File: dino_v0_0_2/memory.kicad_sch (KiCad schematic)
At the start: 5 parts, among them U19 74LS245, U21 74LS245, U24 AT28C256, U26 MCM60256AP, U51 7400

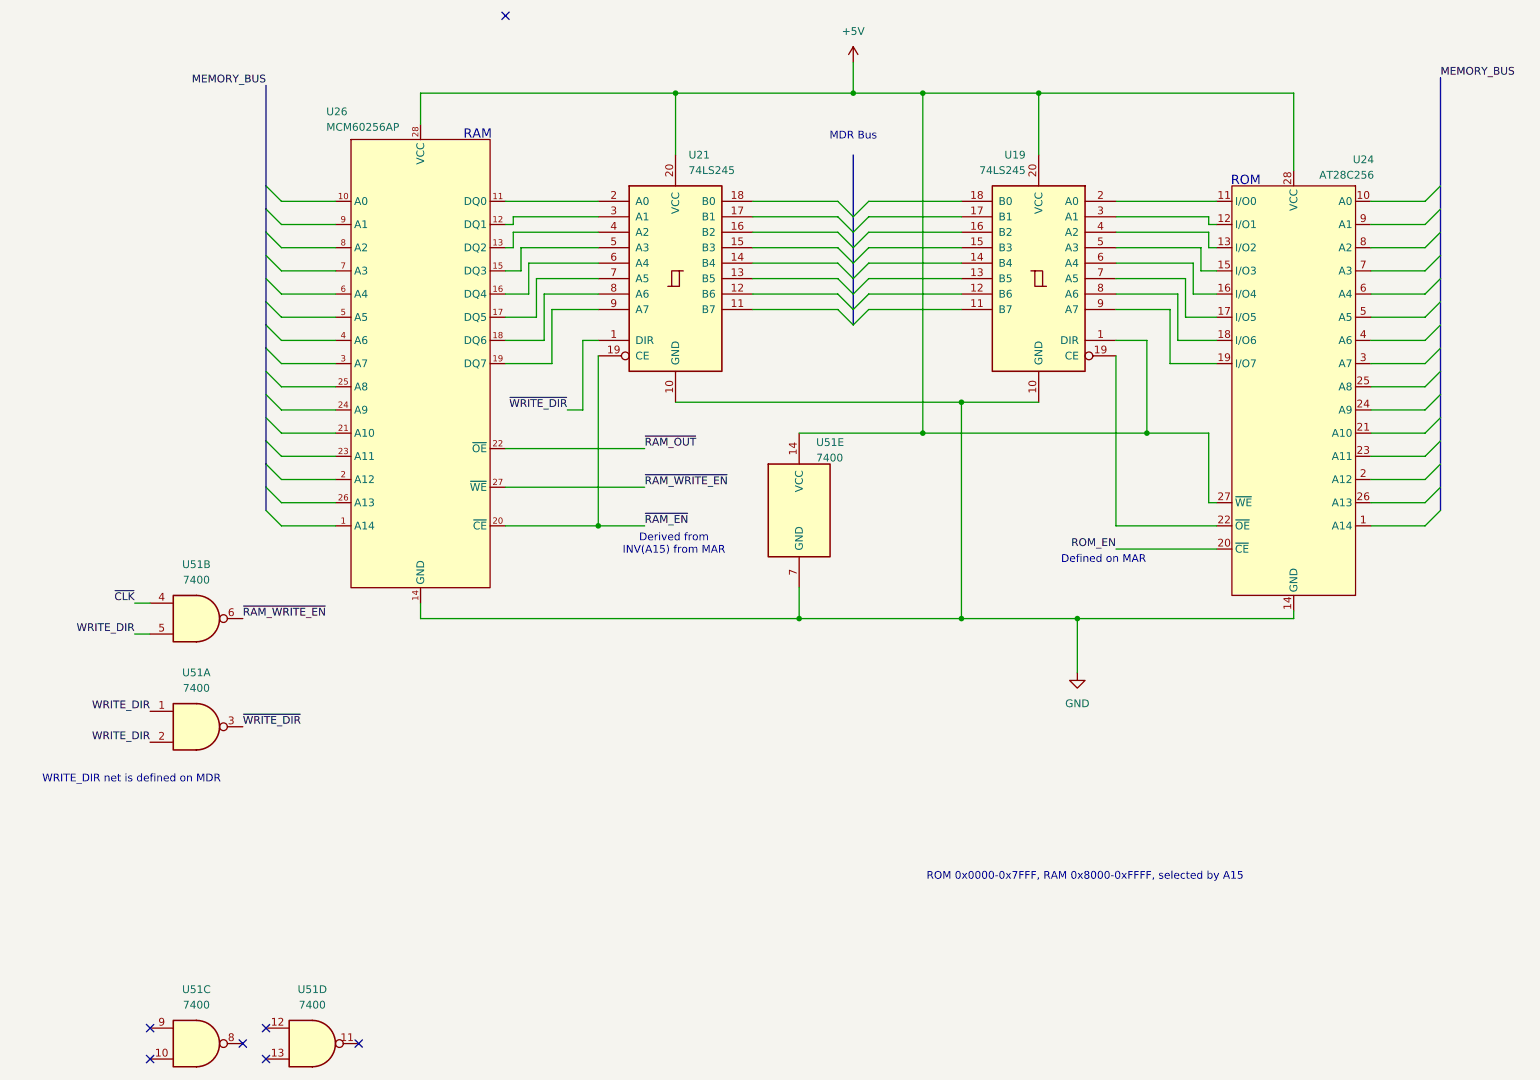
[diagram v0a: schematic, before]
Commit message: DINO v0.0.3: complete ALU/control-word, add MAR+reset sheets, wire reset circuit
ALU sheet: flags register moved from '173 (not in stock) to '273 + a '157
mux to emulate the missing load-enable pins; Z-detect built from a NOR+AND
De Morgan tree instead of a '260; ALU_CIN built from NAND(SA1,SA0) reusing
two already-placed spare gates instead of a dedicated XOR/'86. Sheet is
now fully wired and netlist-clean.

Control word sheet: all 16 CW bits assigned and wired (3x '138 decoders
for the load/source/misc fields, direct bus taps for HALT/PC_MAR_MUX/
PC_UP/END and the ALU SA[2:0] select). Found and fixed several cross-
sheet signal-name mismatches this uncovered (OUT_REG_LOAD/REG_OUT_LOAD,
PC_MAR_MUX/PC_MUX, T-state counter labels, a mirror-reversed IRB->ROM-
address buffer in microcode).

New: MAR and reset sheets, wired into the root hierarchy. Reset circuit
is a from-scratch design: RC+button+74HC14 Schmitt front end feeds the
async PRESET of the clock cluster's spare '74 half (U27B), synchronizing
release to CLK; its Q/~Q fan out to the flags register, the T-state
counter's clear, and (OR'd with the existing microcode-driven PC_CLEAR,
reusing spare gates on the same '02) the PC counters' clear.

Deprecated 7 schematic files no longer referenced by the root sheet's
hierarchy into dino_v0_0_2/deprecated/. Added docs/notes/kicad_netlist.py,
a .kicad_sch connectivity auditor (pin/net resolution incl. buses and
same-name local-label merging) used throughout this session to find the
above bugs; archived completed-work docs into docs/notes/Done/ and
rewrote dino_session_state.md as the current authoritative state+TODO.

Co-Authored-By: Claude Sonnet 5 <noreply@anthropic.com>
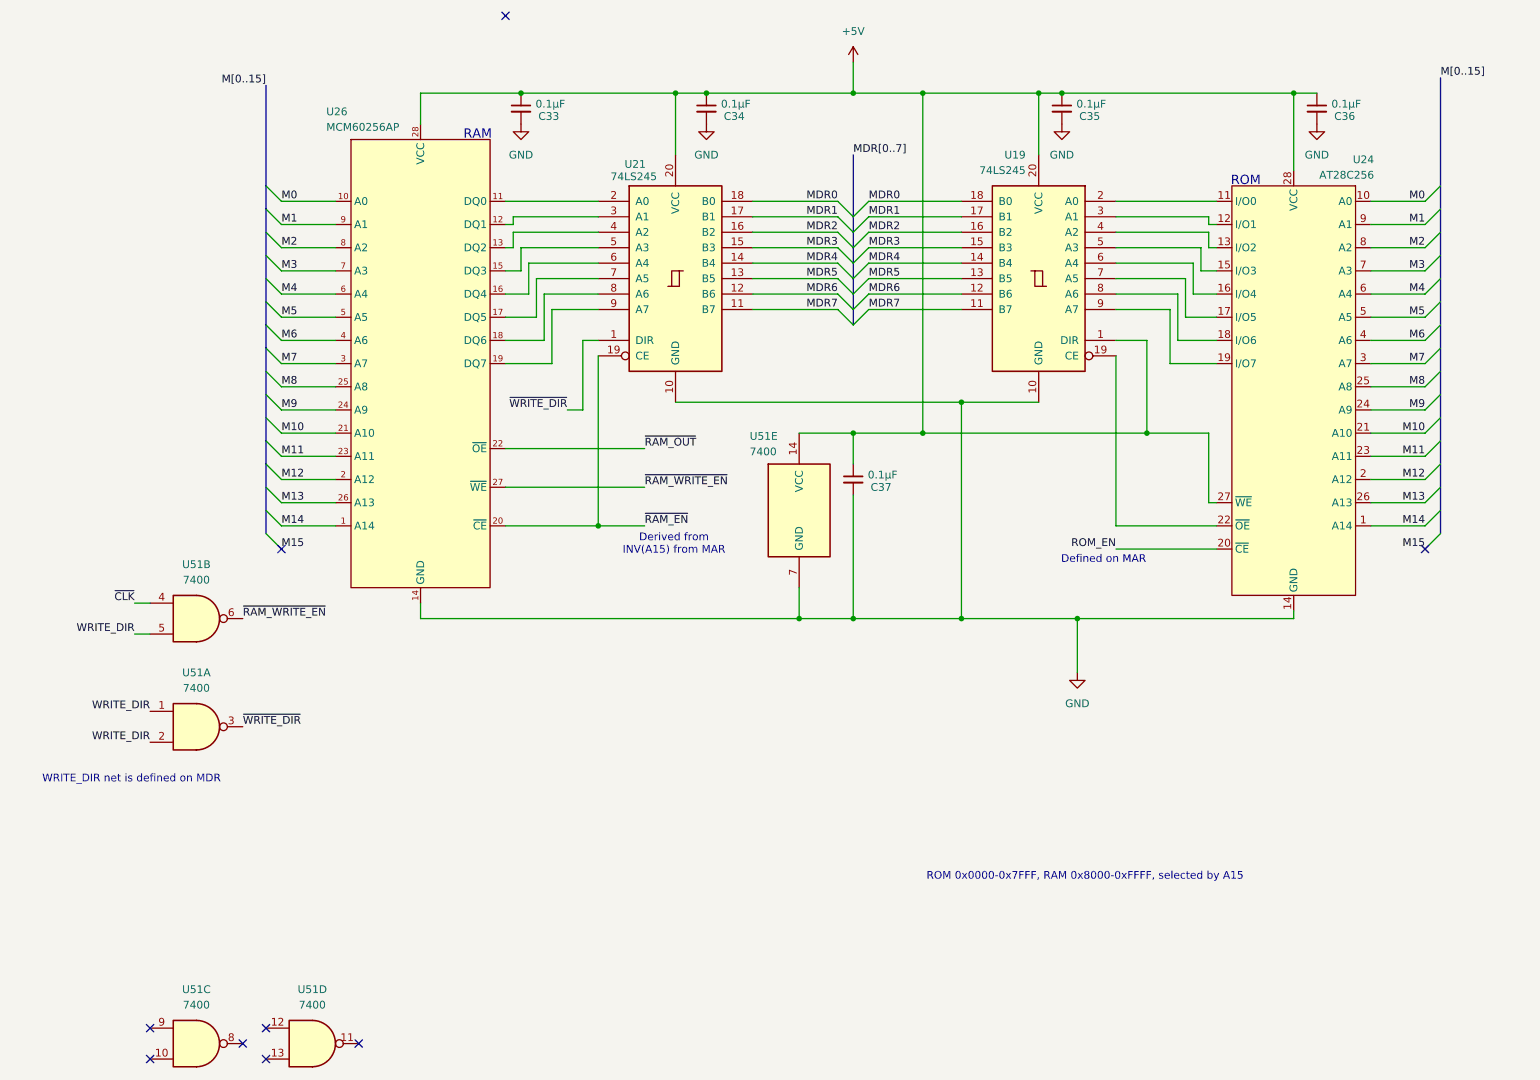
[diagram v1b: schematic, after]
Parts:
- added C33, C34, C35, C36, C37: 0.1µF, symbol Device:C_Small
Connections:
- net +5V: now also C33.1, C34.1, C35.1, C36.1, C37.1
- net GND: now also C33.2, C34.2, C35.2, C36.2, C37.2
- net M14: now reaches U26.1 (A14)
- net M14: now also U24.1 (A14)
- net M0: now reaches U26.10 (A0)
- net M0: now also U24.10 (A0)
- net M12: now reaches U26.2 (A12)
- net M12: now also U24.2 (A12)
- net M10: now reaches U26.21 (A10)
- net M10: now also U24.21 (A10)
- net M11: now reaches U26.23 (A11)
- net M11: now also U24.23 (A11)
- net M9: now reaches U26.24 (A9)
- net M9: now also U24.24 (A9)
- net M8: now reaches U26.25 (A8)
- net M8: now also U24.25 (A8)
- net M13: now reaches U26.26 (A13)
- net M13: now also U24.26 (A13)
- net M7: now reaches U26.3 (A7)
- net M7: now also U24.3 (A7)
- net M6: now reaches U26.4 (A6)
- net M6: now also U24.4 (A6)
- net M5: now reaches U26.5 (A5)
- net M5: now also U24.5 (A5)
- net M4: now reaches U26.6 (A4)
- net M4: now also U24.6 (A4)
- net M3: now reaches U26.7 (A3)
- net M3: now also U24.7 (A3)
- net M2: now reaches U26.8 (A2)
- net M2: now also U24.8 (A2)
- net M1: now reaches U26.9 (A1)
- net M1: now also U24.9 (A1)
- net MDR7: now reaches U21.11 (B7)
- net MDR7: now also U19.11 (B7)
- net MDR6: now reaches U21.12 (B6)
- net MDR6: now also U19.12 (B6)
- net MDR5: now reaches U21.13 (B5)
- net MDR5: now also U19.13 (B5)
- net MDR4: now reaches U21.14 (B4)
- net MDR4: now also U19.14 (B4)
- net MDR3: now reaches U21.15 (B3)
- net MDR3: now also U19.15 (B3)
- net MDR2: now reaches U21.16 (B2)
- net MDR2: now also U19.16 (B2)
- net MDR1: now reaches U21.17 (B1)
- net MDR1: now also U19.17 (B1)
- net MDR0: now reaches U21.18 (B0)
- net MDR0: now also U19.18 (B0)
- no-connect marks 7 -> 9
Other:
- note removed: "MDR Bus"
